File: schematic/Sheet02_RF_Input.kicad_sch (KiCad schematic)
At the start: 4 parts

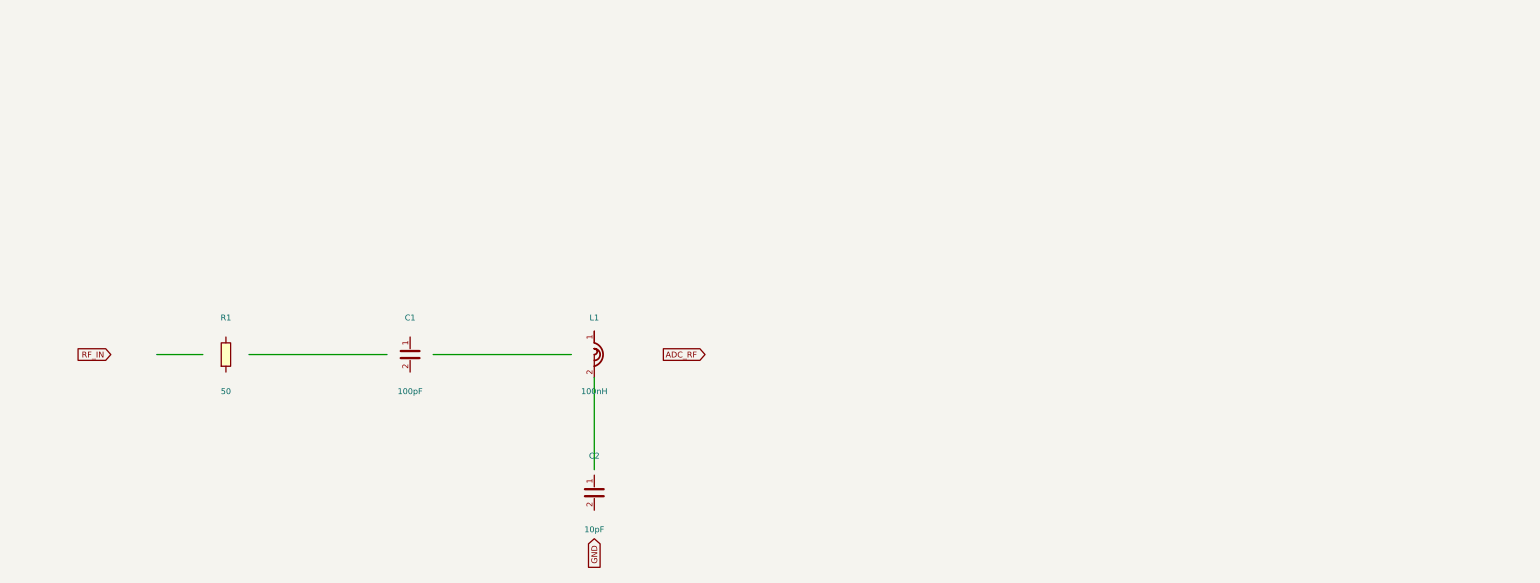
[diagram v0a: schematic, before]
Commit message: feat: real IC schematics with proper pin connections
- ADC12DJ5200-SP: 20 left pins (power, SPI, analog) + 21 right pins (JESD204C)
- XQRVC1902-SP: 19 left pins (power) + 30 right pins (JTAG, SPW, JESD, config)
- TPS7H5002-SP: 9 left + 7 right pins (buck converter 1.0V core)
- ISL70003ASEH: 7 left + 5 right (buck 1.8V/3.3V)
- LMX2615-SP: 8+8 pins (PLL synthesizer)
- LMK04832-SP: 12+12 pins (clock distributor)
- TPS7H1111-SP / TPS7H1121-SP: 3+3 pins (LDOs)
- TPS7H3014-SP: 4+4 pins (sequencer)
- INA214-SP: 3+2 pins (current sense)
- CVHD-950: 3+2 pins (VCXO)

Sheets:
- 02: SMA→50Ω match→anti-alias→ADC analog input
- 03: ADC decoupling, JESD outputs, SPI control
- 04: FPGA 14x decoupling caps, JTAG, SPW, JESD
- 05: Crystek→LMX2615→LMK04832→ADC+FPGA clock tree
- 06-09: Power input, TPS7H5002 buck 1.0V, ISL70003A buck 1.8V/3.3V
- 10-12: LDO 1.0V analog, 1.8V digital, 2.5V clock
- 13: 2x TPS7H3014 power sequencer
- 14: JTAG/SPW/UART connectors
- 15-17: Test points, decoupling, power tree diagram

All 17 sheets export via kicad-cli, merged PDF: 1.1MB
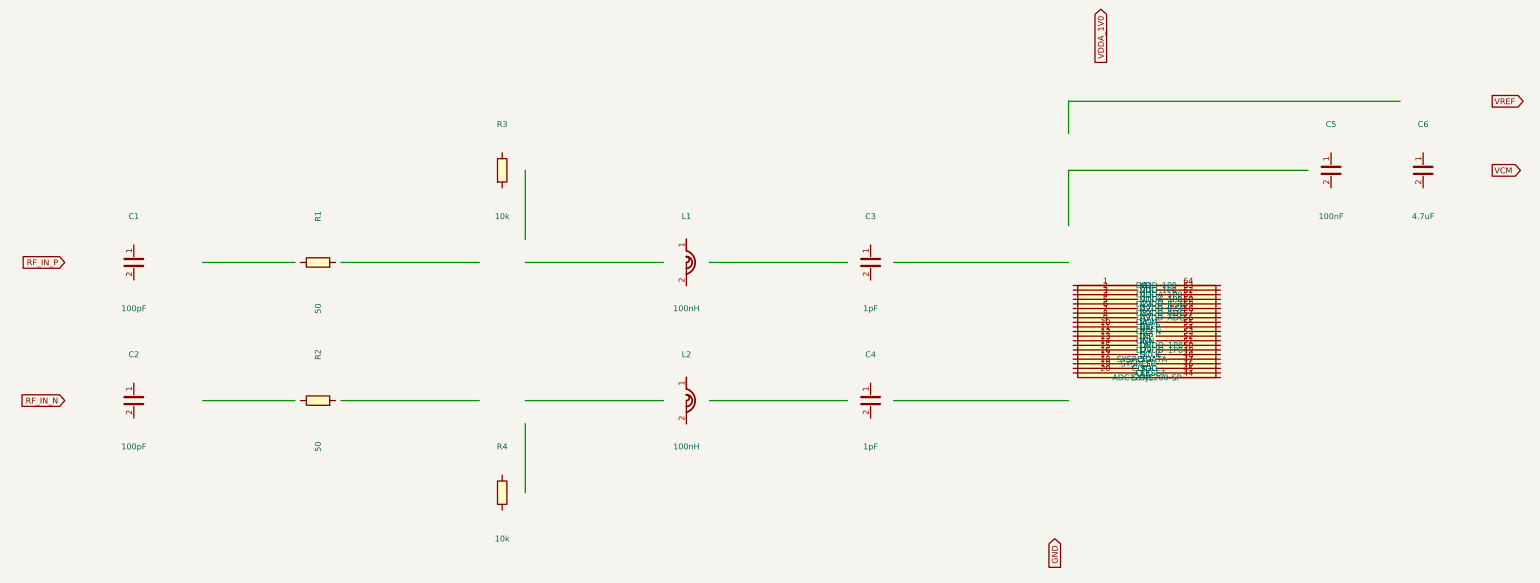
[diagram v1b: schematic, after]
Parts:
- added C3, C4: 1pF, C_0402, symbol Device:C
- added C5: 100nF, C_0402, symbol Device:C
- added C6: 4.7uF, C_0402, symbol Device:C
- added L2: 100nH, L_0402, symbol Device:L
- added R2: 50, R_0402, symbol Device:R
- added R3, R4: 10k, R_0402, symbol Device:R
- added U1: ADC12DJ5200-SP, QFN-64, symbol Custom:ADC12DJ5200-SP
- C1: footprint Capacitor_SMD:C_0402_1005Metric -> C_0402
- C2: value 10pF -> 100pF; footprint Capacitor_SMD:C_0402_1005Metric -> C_0402
- L1: footprint Inductor_SMD:L_0402_1005Metric -> L_0402
- R1: footprint Resistor_SMD:R_0402_1005Metric -> R_0402
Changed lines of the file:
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@@
     (rev "1.0")
   )
-  (symbol (lib_id "Device:R") (at 80 80 0) (unit 1)
+  (symbol (lib_id "Device:C") (at 60 60 0) (unit 1)
     (in_bom yes) (on_board yes)
-    (property "Reference" "R1" (at 80 72 0) (effects (font (size 1.27 1.27))))
-    (property "Value" "50" (at 80 88 0) (effects (font (size 1.27 1.27))))
-    (property "Footprint" "Resistor_SMD:R_0402_1005Metric" (at 80 80 0) (effects (font (size 1.27 1.27)) hide))
+    (property "Reference" "C1" (at 60 50 0) (effects (font (size 1.27 1.27))))
+    (property "Value" "100pF" (at 60 70 0) (effects (font (size 1.27 1.27))))
+    (property "Footprint" "C_0402" (at 60 60 0) (effects (font (size 1.27 1.27)) hide))
     (pin "1")
     (pin "2")
   )
-  (symbol (lib_id "Device:C") (at 120 80 0) (unit 1)
+  (symbol (lib_id "Device:C") (at 60 90 0) (unit 1)
     (in_bom yes) (on_board yes)
-    (property "Reference" "C1" (at 120 72 0) (effects (font (size 1.27 1.27))))
-    (property "Value" "100pF" (at 120 88 0) (effects (font (size 1.27 1.27))))
-    (property "Footprint" "Capacitor_SMD:C_0402_1005Metric" (at 120 80 0) (effects (font (size 1.27 1.27)) hide))
+    (property "Reference" "C2" (at 60 80 0) (effects (font (size 1.27 1.27))))
+    (property "Value" "100pF" (at 60 100 0) (effects (font (size 1.27 1.27))))
+    (property "Footprint" "C_0402" (at 60 90 0) (effects (font (size 1.27 1.27)) hide))
     (pin "1")
     (pin "2")
   )
-  (symbol (lib_id "Device:L") (at 160 80 0) (unit 1)
+  (symbol (lib_id "Device:R") (at 100 60 90) (unit 1)
     (in_bom yes) (on_board yes)
-    (property "Reference" "L1" (at 160 72 0) (effects (font (size 1.27 1.27))))
-    (property "Value" "100nH" (at 160 88 0) (effects (font (size 1.27 1.27))))
-    (property "Footprint" "Inductor_SMD:L_0402_1005Metric" (at 160 80 0) (effects (font (size 1.27 1.27)) hide))
+    (property "Reference" "R1" (at 100 50 0) (effects (font (size 1.27 1.27))))
+    (property "Value" "50" (at 100 70 0) (effects (font (size 1.27 1.27))))
+    (property "Footprint" "R_0402" (at 100 60 0) (effects (font (size 1.27 1.27)) hide))
     (pin "1")
     (pin "2")
   )
-  (symbol (lib_id "Device:C") (at 160 110 0) (unit 1)
+  (symbol (lib_id "Device:R") (at 100 90 90) (unit 1)
     (in_bom yes) (on_board yes)
-    (property "Reference" "C2" (at 160 102 0) (effects (font (size 1.27 1.27))))
-    (property "Value" "10pF" (at 160 118 0) (effects (font (size 1.27 1.27))))
-    (property "Footprint" "Capacitor_SMD:C_0402_1005Metric" (at 160 110 0) (effects (font (size 1.27 1.27)) hide))
+    (property "Reference" "R2" (at 100 80 0) (effects (font (size 1.27 1.27))))
+    (property "Value" "50" (at 100 100 0) (effects (font (size 1.27 1.27))))
+    (property "Footprint" "R_0402" (at 100 90 0) (effects (font (size 1.27 1.27)) hide))
     (pin "1")
     (pin "2")
   )
-  (wire (pts (xy 65 80) (xy 75 80)) (stroke (width 0) (type default)))
-  (wire (pts (xy 85 80) (xy 115 80)) (stroke (width 0) (type default)))
-  (wire (pts (xy 125 80) (xy 155 80)) (stroke (width 0) (type default)))
-  (wire (pts (xy 160 85) (xy 160 105)) (stroke (width 0) (type default)))
-  (global_label "RF_IN" (shape input) (at 55 80 180) (effects (font (size 1.27 1.27)) (justify right)))
-  (global_label "ADC_RF" (shape output) (at 175 80 0) (effects (font (size 1.27 1.27)) (justify left)))
-  (global_label "GND" (shape input) (at 160 120 90) (effects (font (size 1.27 1.27)) (justify right)))
+  (symbol (lib_id "Device:R") (at 140 40 0) (unit 1)
+    (in_bom yes) (on_board yes)
+    (property "Reference" "R3" (at 140 30 0) (effects (font (size 1.27 1.27))))
+    (property "Value" "10k" (at 140 50 0) (effects (font (size 1.27 1.27))))
+    (property "Footprint" "R_0402" (at 140 40 0) (effects (font (size 1.27 1.27)) hide))
+    (pin "1")
+    (pin "2")
+  )
+  (symbol (lib_id "Device:R") (at 140 110 0) (unit 1)
+    (in_bom yes) (on_board yes)
+    (property "Reference" "R4" (at 140 100 0) (effects (font (size 1.27 1.27))))
+    (property "Value" "10k" (at 140 120 0) (effects (font (size 1.27 1.27))))
+    (property "Footprint" "R_0402" (at 140 110 0) (effects (font (size 1.27 1.27)) hide))
+    (pin "1")
+    (pin "2")
+  )
+  (symbol (lib_id "Device:L") (at 180 60 0) (unit 1)
+    (in_bom yes) (on_board yes)
+    (property "Reference" "L1" (at 180 50 0) (effects (font (size 1.27 1.27))))
+    (property "Value" "100nH" (at 180 70 0) (effects (font (size 1.27 1.27))))
+    (property "Footprint" "L_0402" (at 180 60 0) (effects (font (size 1.27 1.27)) hide))
+    (pin "1")
+    (pin "2")
+  )
+  (symbol (lib_id "Device:L") (at 180 90 0) (unit 1)
+    (in_bom yes) (on_board yes)
+    (property "Reference" "L2" (at 180 80 0) (effects (font (size 1.27 1.27))))
+    (property "Value" "100nH" (at 180 100 0) (effects (font (size 1.27 1.27))))
+    (property "Footprint" "L_0402" (at 180 90 0) (effects (font (size 1.27 1.27)) hide))
+    (pin "1")
+    (pin "2")
+  )
+  (symbol (lib_id "Device:C") (at 220 60 0) (unit 1)
+    (in_bom yes) (on_board yes)
+    (property "Reference" "C3" (at 220 50 0) (effects (font (size 1.27 1.27))))
+    (property "Value" "1pF" (at 220 70 0) (effects (font (size 1.27 1.27))))
+    (property "Footprint" "C_0402" (at 220 60 0) (effects (font (size 1.27 1.27)) hide))
+    (pin "1")
+    (pin "2")
+  )
+  (symbol (lib_id "Device:C") (at 220 90 0) (unit 1)
+    (in_bom yes) (on_board yes)
+    (property "Reference" "C4" (at 220 80 0) (effects (font (size 1.27 1.27))))
+    (property "Value" "1pF" (at 220 100 0) (effects (font (size 1.27 1.27))))
+    (property "Footprint" "C_0402" (at 220 90 0) (effects (font (size 1.27 1.27)) hide))
+    (pin "1")
+    (pin "2")
+  )
+  (symbol (lib_id "Custom:ADC12DJ5200-SP") (at 280 75 0) (unit 1)
+    (in_bom yes) (on_board yes)
+    (property "Reference" "U1" (at 280 65 0) (effects (font (size 1.27 1.27))))
+    (property "Value" "ADC12DJ5200-SP" (at 280 85 0) (effects (font (size 1.27 1.27))))
+    (property "Footprint" "QFN-64" (at 280 75 0) (effects (font (size 1.27 1.27)) hide))
+    (pin "1")
+    (pin "2")
+    (pin "3")
+    (pin "4")
+    (pin "5")
+    (pin "6")
+    (pin "7")
+    (pin "8")
+    (pin "9")
+    (pin "10")
+    (pin "11")
+    (pin "12")
+    (pin "13")
+    (pin "14")
+    (pin "15")
+    (pin "16")
+    (pin "17")
+    (pin "18")
+    (pin "19")
+    (pin "20")
+    (pin "21")
+    (pin "22")
+    (pin "23")
+    (pin "24")
+    (pin "25")
+    (pin "26")
+    (pin "27")
+    (pin "28")
+    (pin "29")
+    (pin "30")
+    (pin "31")
+    (pin "32")
+    (pin "33")
+    (pin "34")
+    (pin "35")
+    (pin "36")
+    (pin "37")
+    (pin "38")
+    (pin "39")
+    (pin "40")
+    (pin "41")
+    (pin "42")
+    (pin "43")
+    (pin "44")
+    (pin "45")
+    (pin "46")
+    (pin "47")
+    (pin "48")
+    (pin "49")
+    (pin "50")
+    (pin "51")
+    (pin "52")
+    (pin "53")
+    (pin "54")
+    (pin "55")
+    (pin "56")
+    (pin "57")
+    (pin "58")
+    (pin "59")
+    (pin "60")
+    (pin "61")
+    (pin "62")
+    (pin "63")
+    (pin "64")
+    (pin "65")
+  )
+  (symbol (lib_id "Device:C") (at 320 40 0) (unit 1)
+    (in_bom yes) (on_board yes)
+    (property "Reference" "C5" (at 320 30 0) (effects (font (size 1.27 1.27))))
+    (property "Value" "100nF" (at 320 50 0) (effects (font (size 1.27 1.27))))
+    (property "Footprint" "C_0402" (at 320 40 0) (effects (font (size 1.27 1.27)) hide))
+    (pin "1")
+    (pin "2")
+  )
+  (symbol (lib_id "Device:C") (at 340 40 0) (unit 1)
+    (in_bom yes) (on_board yes)
+    (property "Reference" "C6" (at 340 30 0) (effects (font (size 1.27 1.27))))
+    (property "Value" "4.7uF" (at 340 50 0) (effects (font (size 1.27 1.27))))
+    (property "Footprint" "C_0402" (at 340 40 0) (effects (font (size 1.27 1.27)) hide))
+    (pin "1")
+    (pin "2")
+  )
+  (wire (pts (xy 75 60) (xy 95 60)) (stroke (width 0) (type default)))
+  (wire (pts (xy 105 60) (xy 135 60)) (stroke (width 0) (type default)))
+  (wire (pts (xy 145 60) (xy 175 60)) (stroke (width 0) (type default)))
+  (wire (pts (xy 185 60) (xy 215 60)) (stroke (width 0) (type default)))
+  (wire (pts (xy 225 60) (xy 263 60)) (stroke (width 0) (type default)))
+  (wire (pts (xy 75 90) (xy 95 90)) (stroke (width 0) (type default)))
+  (wire (pts (xy 105 90) (xy 135 90)) (stroke (width 0) (type default)))
+  (wire (pts (xy 145 90) (xy 175 90)) (stroke (width 0) (type default)))
+  (wire (pts (xy 185 90) (xy 215 90)) (stroke (width 0) (type default)))
+  (wire (pts (xy 225 90) (xy 263 90)) (stroke (width 0) (type default)))
+  (wire (pts (xy 145 40) (xy 145 55)) (stroke (width 0) (type default)))
+  (wire (pts (xy 145 110) (xy 145 95)) (stroke (width 0) (type default)))
+  (wire (pts (xy 263 52) (xy 263 40)) (stroke (width 0) (type default)))
+  (wire (pts (xy 263 40) (xy 315 40)) (stroke (width 0) (type default)))
+  (wire (pts (xy 263 32) (xy 263 25)) (stroke (width 0) (type default)))
+  (wire (pts (xy 263 25) (xy 335 25)) (stroke (width 0) (type default)))
+  (global_label "RF_IN_P" (shape input) (at 45 60 180) (effects (font (size 1.27 1.27)) (justify right)))
+  (global_label "RF_IN_N" (shape input) (at 45 90 180) (effects (font (size 1.27 1.27)) (justify right)))
+  (global_label "VCM" (shape output) (at 355 40 0) (effects (font (size 1.27 1.27)) (justify left)))
+  (global_label "VREF" (shape output) (at 355 25 0) (effects (font (size 1.27 1.27)) (justify left)))
+  (global_label "VDDA_1V0" (shape input) (at 270 5 270) (effects (font (size 1.27 1.27)) (justify right)))
+  (global_label "GND" (shape input) (at 260 120 90) (effects (font (size 1.27 1.27)) (justify right)))
   (sheet_instances (path "/" (page "1")))
 )
